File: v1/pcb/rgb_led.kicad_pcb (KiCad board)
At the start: 2 copper layers, 62.7 x 45.2 mm, 7 parts, among them P1 CONN_2, P2 CONN_4

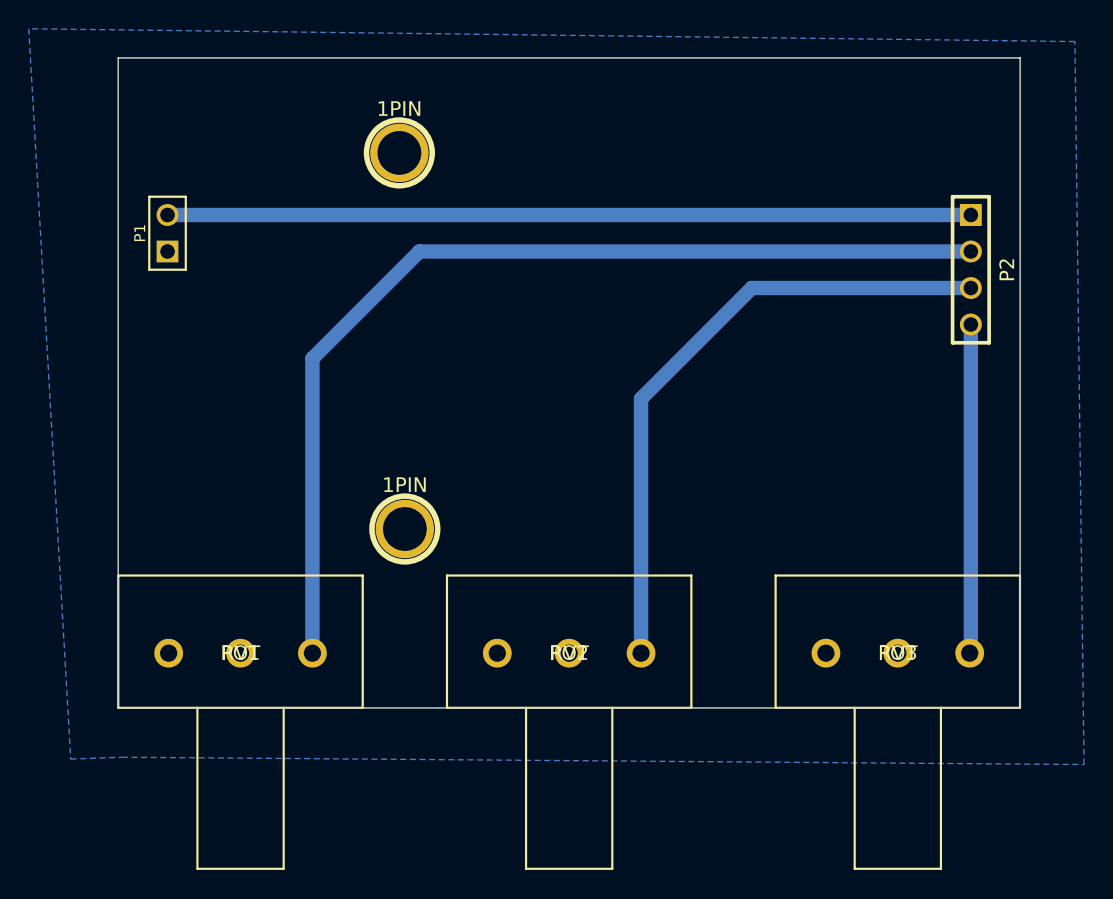
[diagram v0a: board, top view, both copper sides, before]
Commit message: v1: Add switch to PCB and make it a bit smaller
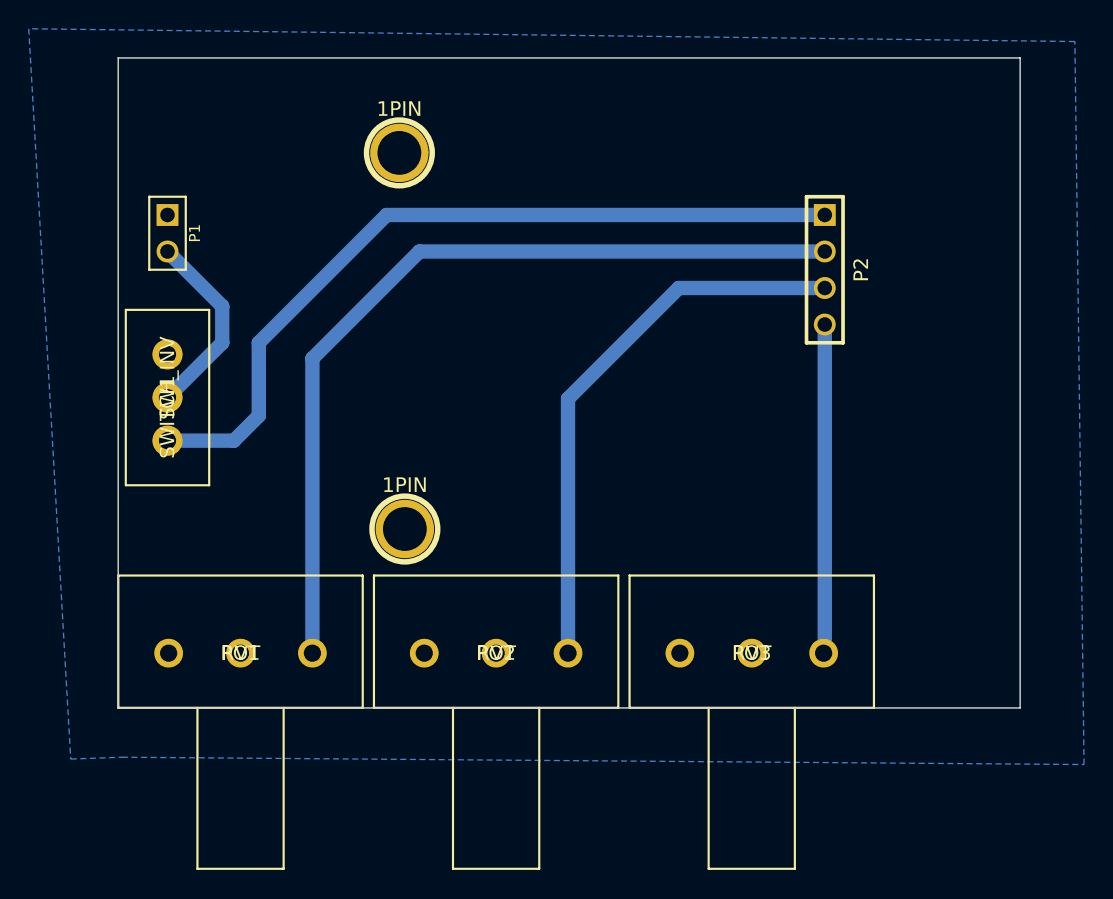
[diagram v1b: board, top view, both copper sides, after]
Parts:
- added SW1: SWITCH_INV, Switch_SS-12F46, F.Cu at (22.9, 35.6)
- moved P2 10.2 mm to (68.6, 26.7)
- moved RV3 10.2 mm to (63.5, 53.3)
- moved RV2 5.08 mm to (45.7, 53.3)
- turned P1 to 270 degrees
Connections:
- P2 pad 1: VDD -> N-000004
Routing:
- net N-000004: track 0.00 -> 55.2 mm
- net VDD: track 55.9 -> 13.3 mm
- net N-000003: track 69.4 -> 59.2 mm
- net N-000002: track 43.8 -> 38.7 mm
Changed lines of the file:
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@@
 (kicad_pcb (version 3) (host pcbnew "(2013-may-18)-stable")
   (general
-    (links 10)
+    (links 11)
     (no_connects 0)
-    (area 13.208 9.906 86.614001 68.669001)
+    (area 19.380999 11.887999 82.219001 57.200001)
     (thickness 1.6)
     (drawings 8)
-    (tracks 9)
+    (tracks 16)
     (zones 0)
-    (modules 7)
-    (nets 6)
+    (modules 8)
+    (nets 7)
   )
   (page A3)
@@
   (net 0 "")
   (net 1 GND)
-  (net 2 N-000002)
-  (net 3 N-000003)
-  (net 4 N-000004)
-  (net 5 VDD)
+  (net 2 N-000001)
+  (net 3 N-000002)
+  (net 4 N-000003)
+  (net 5 N-000004)
+  (net 6 VDD)
   (net_class Default "This is the default net class."
     (clearance 0.254)
@@
     (add_net "")
     (add_net GND)
+    (add_net N-000001)
     (add_net N-000002)
     (add_net N-000003)
@@
   )
   (module POT_3 (layer F.Cu)
-    (at 50.8 53.34)
+    (at 45.72 53.34)
     (fp_text reference RV2 (at 0 0) (layer F.SilkS)
       (effects (font (size 1 1) (thickness 0.15)))
@@
     (pad 3 thru_hole circle (at 5 0) (size 2 2) (drill 1.2)
       (layers *.Cu *.Mask F.SilkS)
-      (net 3 N-000003)
+      (net 3 N-000002)
     )
   )
   (module POT_3 (layer F.Cu)
-    (at 73.66 53.34)
+    (at 63.5 53.34)
     (fp_text reference RV3 (at 0 0) (layer F.SilkS)
       (effects (font (size 1 1) (thickness 0.15)))
@@
     (pad 3 thru_hole circle (at 5 0) (size 2 2) (drill 1.2)
       (layers *.Cu *.Mask F.SilkS)
-      (net 4 N-000004)
+      (net 2 N-000001)
     )
   )
@@
     (pad 3 thru_hole circle (at 5 0) (size 2 2) (drill 1.2)
       (layers *.Cu *.Mask F.SilkS)
-      (net 2 N-000002)
+      (net 4 N-000003)
     )
   )
   (module PIN_ARRAY_4x1 (layer F.Cu)
-    (at 78.74 26.67 270)
+    (at 68.58 26.67 270)
     (descr "Double rangee de contacts 2 x 5 pins")
     (tags CONN)
@@
     (pad 1 thru_hole rect (at -3.81 0 270) (size 1.524 1.524) (drill 1.016)
       (layers *.Cu *.Mask F.SilkS)
-      (net 5 VDD)
+      (net 5 N-000004)
     )
     (pad 2 thru_hole circle (at -1.27 0 270) (size 1.524 1.524) (drill 1.016)
       (layers *.Cu *.Mask F.SilkS)
-      (net 2 N-000002)
+      (net 4 N-000003)
     )
     (pad 3 thru_hole circle (at 1.27 0 270) (size 1.524 1.524) (drill 1.016)
       (layers *.Cu *.Mask F.SilkS)
-      (net 3 N-000003)
+      (net 3 N-000002)
     )
     (pad 4 thru_hole circle (at 3.81 0 270) (size 1.524 1.524) (drill 1.016)
       (layers *.Cu *.Mask F.SilkS)
-      (net 4 N-000004)
+      (net 2 N-000001)
     )
     (model pin_array\pins_array_4x1.wrl
@@
   )
   (module PIN_ARRAY_2X1 (layer F.Cu)
-    (at 22.86 24.13 90)
+    (at 22.86 24.13 270)
     (descr "Connecteurs 2 pins")
     (tags "CONN DEV")
-    (fp_text reference P1 (at 0 -1.905 90) (layer F.SilkS)
+    (fp_text reference P1 (at 0 -1.905 270) (layer F.SilkS)
       (effects (font (size 0.762 0.762) (thickness 0.1524)))
     )
-    (fp_text value CONN_2 (at 0 -1.905 90) (layer F.SilkS) hide
+    (fp_text value CONN_2 (at 0 -1.905 270) (layer F.SilkS) hide
       (effects (font (size 0.762 0.762) (thickness 0.1524)))
     )
@@
     (fp_line (start 2.54 -1.27) (end 2.54 1.27) (layer F.SilkS) (width 0.1524))
     (fp_line (start 2.54 1.27) (end -2.54 1.27) (layer F.SilkS) (width 0.1524))
-    (pad 1 thru_hole rect (at -1.27 0 90) (size 1.524 1.524) (drill 1.016)
-      (layers *.Cu *.Mask F.SilkS)
-      (net 1 GND)
-    )
-    (pad 2 thru_hole circle (at 1.27 0 90) (size 1.524 1.524) (drill 1.016)
-      (layers *.Cu *.Mask F.SilkS)
-      (net 5 VDD)
+    (pad 1 thru_hole rect (at -1.27 0 270) (size 1.524 1.524) (drill 1.016)
+      (layers *.Cu *.Mask F.SilkS)
+      (net 1 GND)
+    )
+    (pad 2 thru_hole circle (at 1.27 0 270) (size 1.524 1.524) (drill 1.016)
+      (layers *.Cu *.Mask F.SilkS)
+      (net 6 VDD)
     )
     (model pin_array/pins_array_2x1.wrl
@@
     )
   )
-  (gr_text Blue (at 73.66 45.339) (layer B.Mask)
+  (module Switch_SS-12F46 (layer F.Cu)
+    (at 22.86 35.56 90)
+    (fp_text reference SW1 (at 0 0 90) (layer F.SilkS)
+      (effects (font (size 1 1) (thickness 0.15)))
+    )
+    (fp_text value SWITCH_INV (at 0 0 90) (layer F.SilkS)
+      (effects (font (size 1 1) (thickness 0.15)))
+    )
+    (fp_line (start -6.1 -2.9) (end 6.1 -2.9) (layer F.SilkS) (width 0.15))
+    (fp_line (start 6.1 -2.9) (end 6.1 2.9) (layer F.SilkS) (width 0.15))
+    (fp_line (start 6.1 2.9) (end -6.1 2.9) (layer F.SilkS) (width 0.15))
+    (fp_line (start -6.1 2.9) (end -6.1 -2.9) (layer F.SilkS) (width 0.15))
+    (pad 1 thru_hole circle (at -3 0 90) (size 2.1 2.1) (drill 1.2)
+      (layers *.Cu *.Mask F.SilkS)
+      (net 5 N-000004)
+    )
+    (pad 2 thru_hole circle (at 0 0 90) (size 2.1 2.1) (drill 1.2)
+      (layers *.Cu *.Mask F.SilkS)
+      (net 6 VDD)
+    )
+    (pad 3 thru_hole circle (at 3 0 90) (size 2.1 2.1) (drill 1.2)
+      (layers *.Cu *.Mask F.SilkS)
+    )
+    (pad "" np_thru_hole oval (at 5.85 0 90) (size 1.2 2.4) (drill oval 0.8 2)
+      (layers *.Cu *.Mask F.SilkS)
+    )
+    (pad "" np_thru_hole oval (at -5.85 0 90) (size 1.2 2.4) (drill oval 0.8 2)
+      (layers *.Cu *.Mask F.SilkS)
+    )
+  )
+  (gr_text Blue (at 63.5 45.72) (layer B.Mask)
     (effects (font (size 1.5 1.5) (thickness 0.3)) (justify mirror))
   )
-  (gr_text Red (at 50.927 45.339) (layer B.Mask)
+  (gr_text Red (at 45.72 45.72) (layer B.Mask)
     (effects (font (size 1.5 1.5) (thickness 0.3)) (justify mirror))
   )
-  (gr_text Green (at 27.94 45.339) (layer B.Mask)
+  (gr_text Green (at 27.94 45.72) (layer B.Mask)
     (effects (font (size 1.5 1.5) (thickness 0.3)) (justify mirror))
   )
@@
   (gr_line (start 82.169 11.938) (end 19.431 11.938) (angle 90) (layer Edge.Cuts) (width 0.1))
   (gr_line (start 82.169 57.15) (end 82.169 11.938) (angle 90) (layer Edge.Cuts) (width 0.1))
-  (segment (start 32.94 53.34) (end 32.94 32.846) (width 1) (layer B.Cu) (net 2))
-  (segment (start 40.386 25.4) (end 78.74 25.4) (width 1) (layer B.Cu) (net 2))
-  (segment (start 32.94 32.846) (end 40.386 25.4) (width 1) (layer B.Cu) (net 2))
-  (segment (start 55.8 53.34) (end 55.8 35.64) (width 1) (layer B.Cu) (net 3))
-  (segment (start 63.5 27.94) (end 78.74 27.94) (width 1) (layer B.Cu) (net 3))
-  (segment (start 55.8 35.64) (end 63.5 27.94) (width 1) (layer B.Cu) (net 3))
-  (segment (start 78.74 30.48) (end 78.74 53.26) (width 1) (layer B.Cu) (net 4))
-  (segment (start 78.74 53.26) (end 78.66 53.34) (width 1) (layer B.Cu) (net 4))
-  (segment (start 22.86 22.86) (end 78.74 22.86) (width 1) (layer B.Cu) (net 5))
+  (segment (start 68.58 53.26) (end 68.5 53.34) (width 1) (layer B.Cu) (net 2))
+  (segment (start 68.58 30.48) (end 68.58 53.26) (width 1) (layer B.Cu) (net 2))
+  (segment (start 50.72 53.34) (end 50.72 35.64) (width 1) (layer B.Cu) (net 3))
+  (segment (start 50.72 35.64) (end 58.42 27.94) (width 1) (layer B.Cu) (net 3))
+  (segment (start 58.42 27.94) (end 68.58 27.94) (width 1) (layer B.Cu) (net 3))
+  (segment (start 32.94 53.34) (end 32.94 32.846) (width 1) (layer B.Cu) (net 4))
+  (segment (start 40.386 25.4) (end 68.58 25.4) (width 1) (layer B.Cu) (net 4))
+  (segment (start 32.94 32.846) (end 40.386 25.4) (width 1) (layer B.Cu) (net 4))
+  (segment (start 68.58 22.86) (end 38.1 22.86) (width 1) (layer B.Cu) (net 5))
+  (segment (start 27.48 38.56) (end 22.86 38.56) (width 1) (layer B.Cu) (net 5))
+  (segment (start 29.21 36.83) (end 27.48 38.56) (width 1) (layer B.Cu) (net 5))
+  (segment (start 29.21 31.75) (end 29.21 36.83) (width 1) (layer B.Cu) (net 5))
+  (segment (start 38.1 22.86) (end 29.21 31.75) (width 1) (layer B.Cu) (net 5))
+  (segment (start 22.86 25.4) (end 26.67 29.21) (width 1) (layer B.Cu) (net 6))
+  (segment (start 26.67 31.75) (end 22.86 35.56) (width 1) (layer B.Cu) (net 6))
+  (segment (start 26.67 29.21) (end 26.67 31.75) (width 1) (layer B.Cu) (net 6))
   (zone (net 1) (net_name GND) (layer B.Cu) (hatch edge 0.508)
     (connect_pads (clearance 0.508))

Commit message: [v1] Adjusted date and version on PCB
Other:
- board text added: "coredump RGB LED V1.1 2015"
- board text removed: "coredump RGB LED V1 2014"
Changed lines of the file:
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@@
     (links 11)
     (no_connects 0)
-    (area 19.380999 11.887999 82.219001 57.200001)
+    (area 13.208 9.906 86.614001 68.669001)
     (thickness 1.6)
     (drawings 8)
@@
     (effects (font (size 1.5 1.5) (thickness 0.3)) (justify mirror))
   )
-  (gr_text "coredump\nRGB LED V1 2014" (at 61.849 15.621) (layer B.Mask)
+  (gr_text "coredump\nRGB LED V1.1 2015" (at 61.849 15.621) (layer B.Mask)
     (effects (font (size 2 2) (thickness 0.3)) (justify mirror))
   )

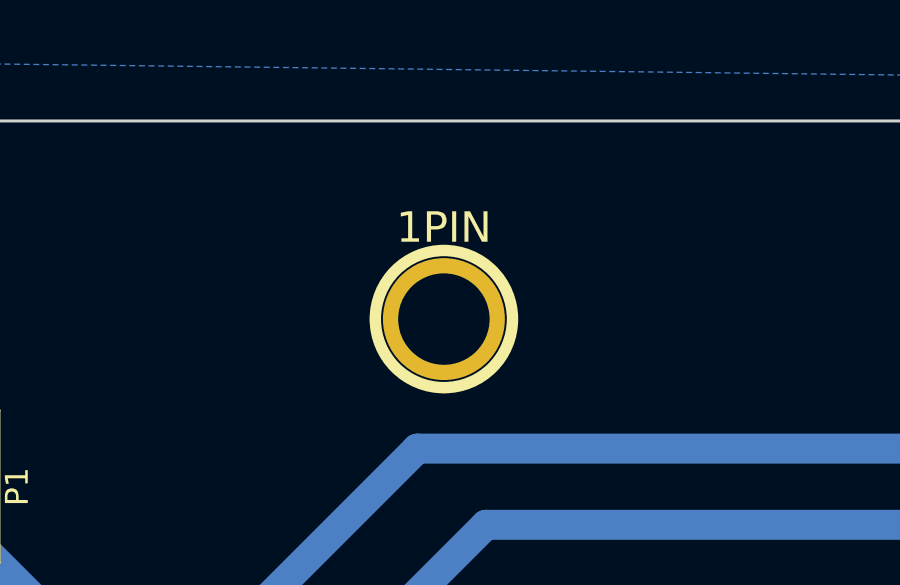
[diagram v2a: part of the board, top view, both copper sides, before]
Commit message: Increased distance between battery holes
9V battery length is 26.5mm.
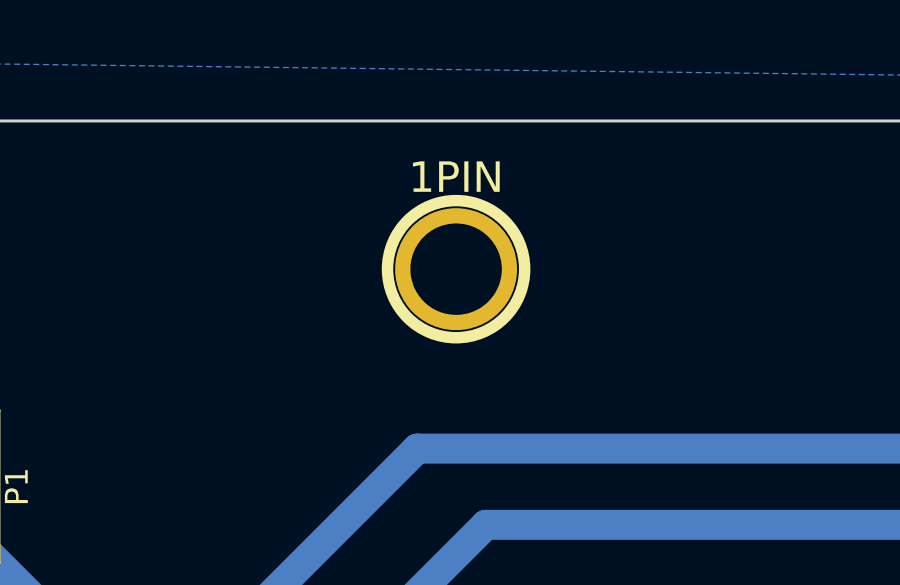
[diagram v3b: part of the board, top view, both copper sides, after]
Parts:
- moved 1PIN 1.71 mm to (39.4, 16.9)
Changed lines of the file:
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@@
   )
   (module 1pin (layer F.Cu)
-    (at 38.989 18.542)
+    (at 39.3954 16.8783)
     (descr "module 1 pin (ou trou mecanique de percage)")
     (tags DEV)
